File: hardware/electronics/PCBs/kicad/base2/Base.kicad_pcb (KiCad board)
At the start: 2 copper layers, 79.4 x 68 mm, 69 parts, among them J14 Conn_01x04, J3 USB_C_Receptacle_USB2.0_16P, SW1 D2LS-21, SW2 D2LS-21, SW3 TS-1088-AR02016, U1 W25Q16JVSSIQ, U2 PMW3360DM-T2QU, U3 AP2202K-3.3, U4 AP2204K-1.8, U6 RP2350A, Y1 ABM8-272-T3

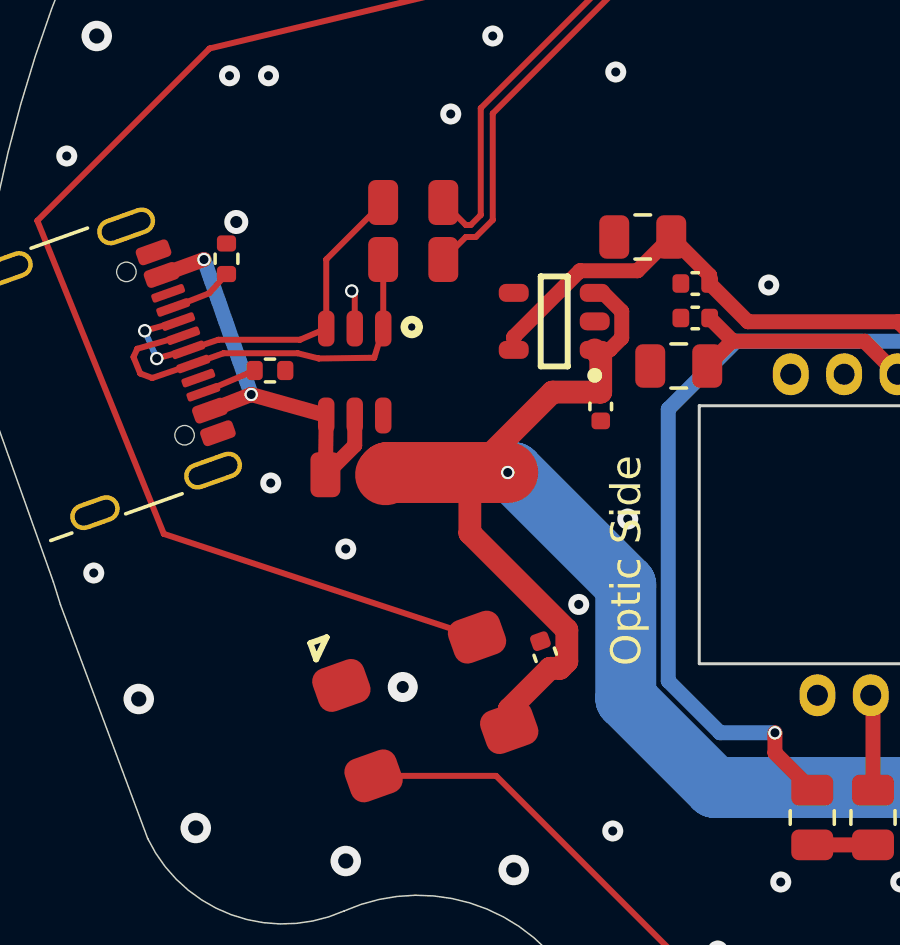
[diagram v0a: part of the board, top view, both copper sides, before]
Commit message: PCB revs. Add vertical rgb leds. Fix sensor cutout
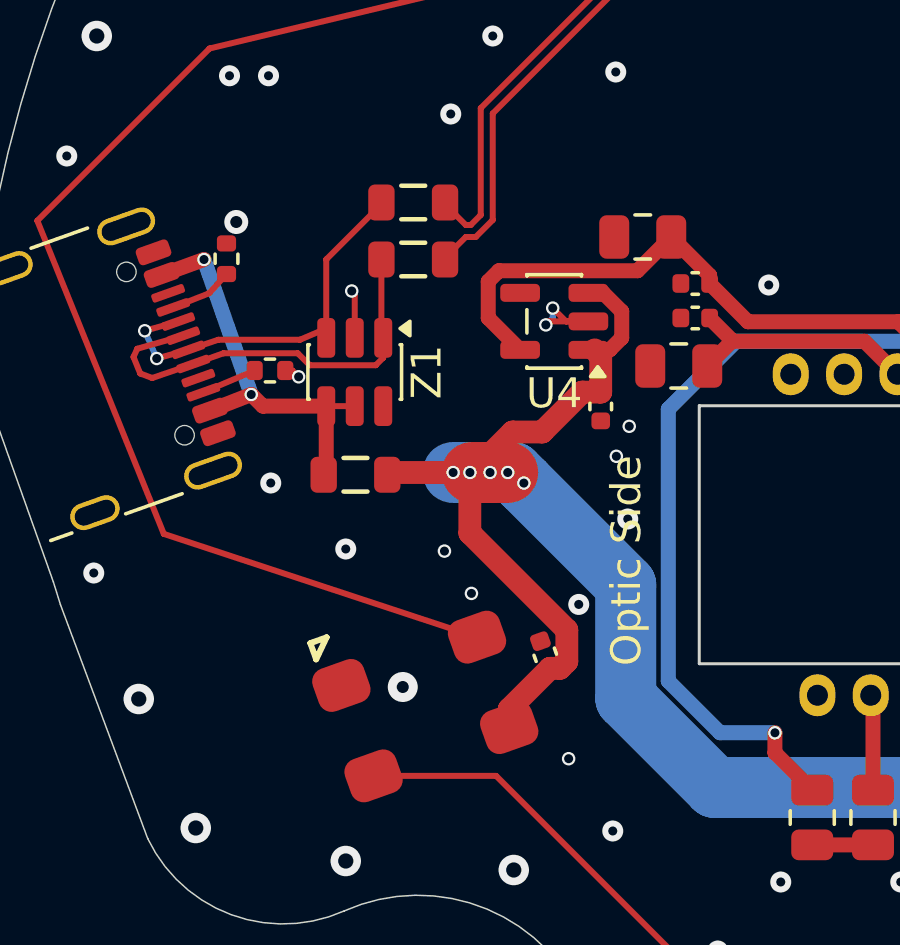
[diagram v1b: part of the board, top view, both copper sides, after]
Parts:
- FB1, FB2, FB3: footprint Chip_Passives:0805 -> PCM_JLCPCB:FB_0805
- U4: footprint PowerSupply:AP2202 - SOT95P270X145-5N -> Package_TO_SOT_SMD:SOT-23-5
- Z1: footprint Diodes:PESD3V3S4UD - SOT95P275X110-6N -> Package_TO_SOT_SMD:SOT-23-6
- turned FB1 to 0 degrees
- turned FB2 to 0 degrees
- turned FB3 to 0 degrees
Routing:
- net GND: track 17.9 -> 22.0 mm, vias 168 -> 176
- net /MOS/1V8: track 45.0 -> 47.4 mm
- net /LED/V_USB: track 169.6 -> 168.0 mm, vias 6 -> 10
- net Net-(FB1-Pad1): track 14.7 -> 13.7 mm
- net Net-(FB3-Pad1): track 13.8 -> 14.3 mm

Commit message: Add the holes back. 🤦
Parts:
- added ?: , , B.Cu at (159.1, 80.5)
- added ?: , , B.Cu at (181.1, 80.5)
- added ?: , , B.Cu at (143.4, 92.6)
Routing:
- net /LED/V_USB: track 168.0 -> 170.7 mm
